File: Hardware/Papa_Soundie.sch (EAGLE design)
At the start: 80 parts, among them J1 Audio Jack, J2 MICRO-SD_CARD_SOCKET, U1 ATMEGA328P_TQFP, U2 VS1000D, U3 3.3V, U4 4MB Flash, Y1 12MHz, Y2 8MHz

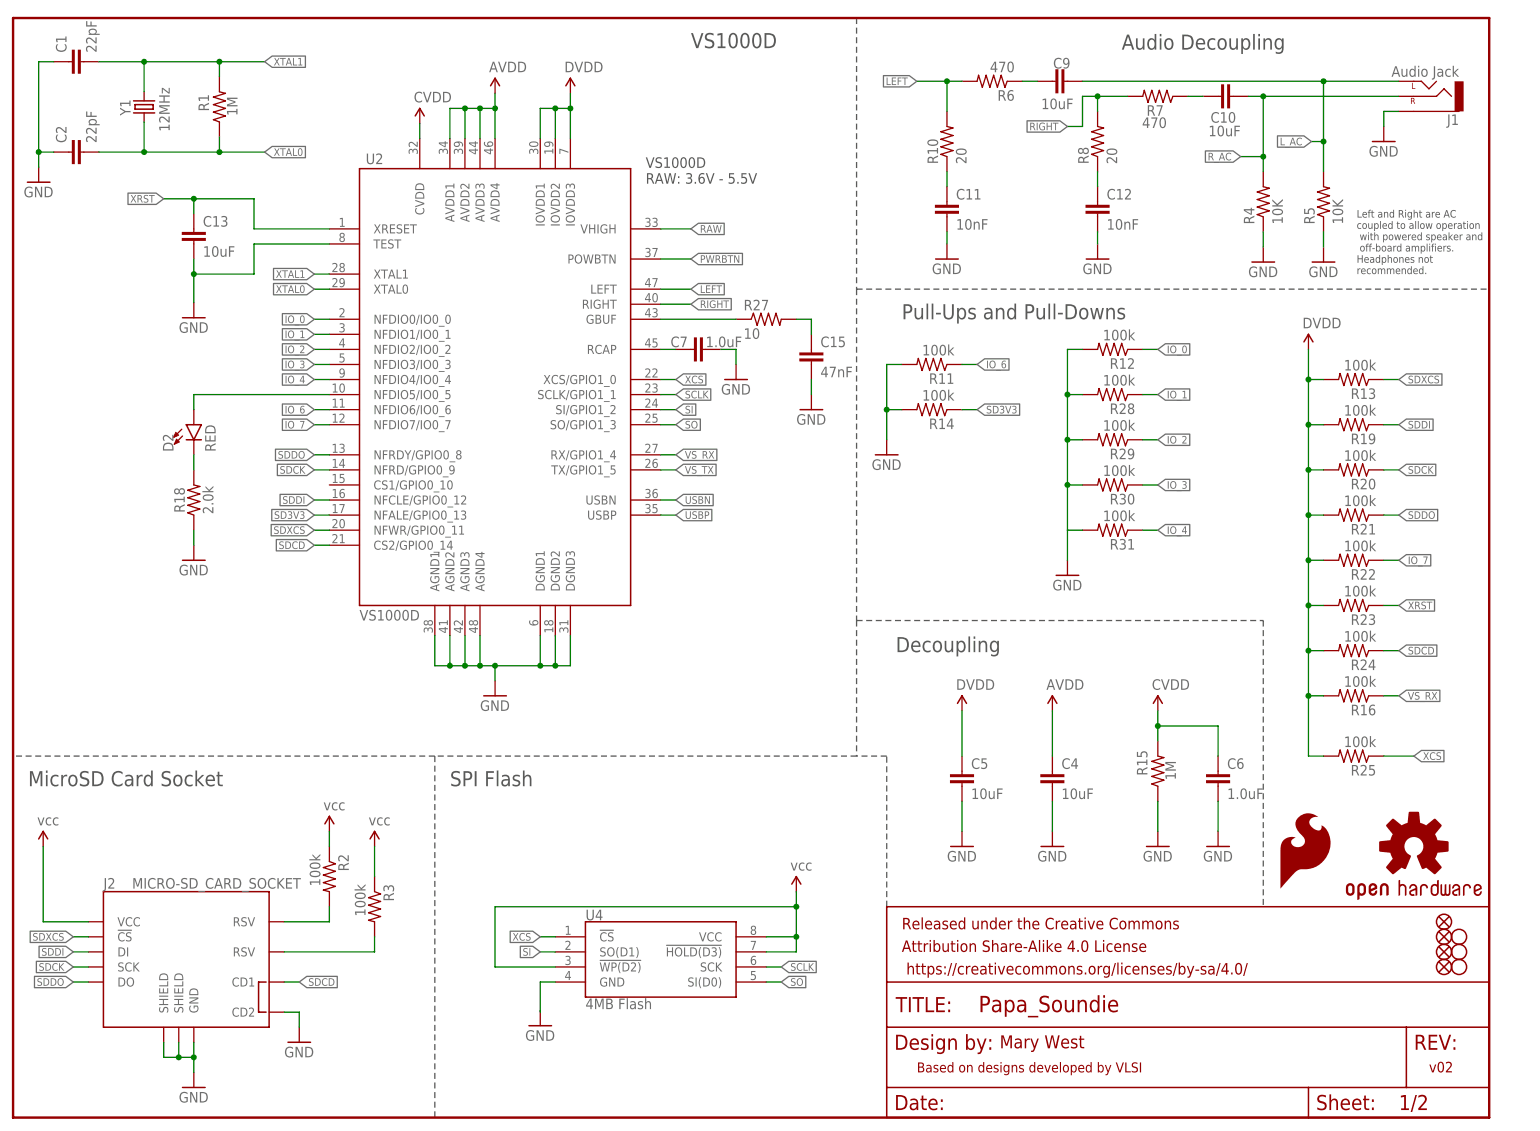
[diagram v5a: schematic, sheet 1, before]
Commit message: Updated Version No., removed ground connection from SD Card, v03
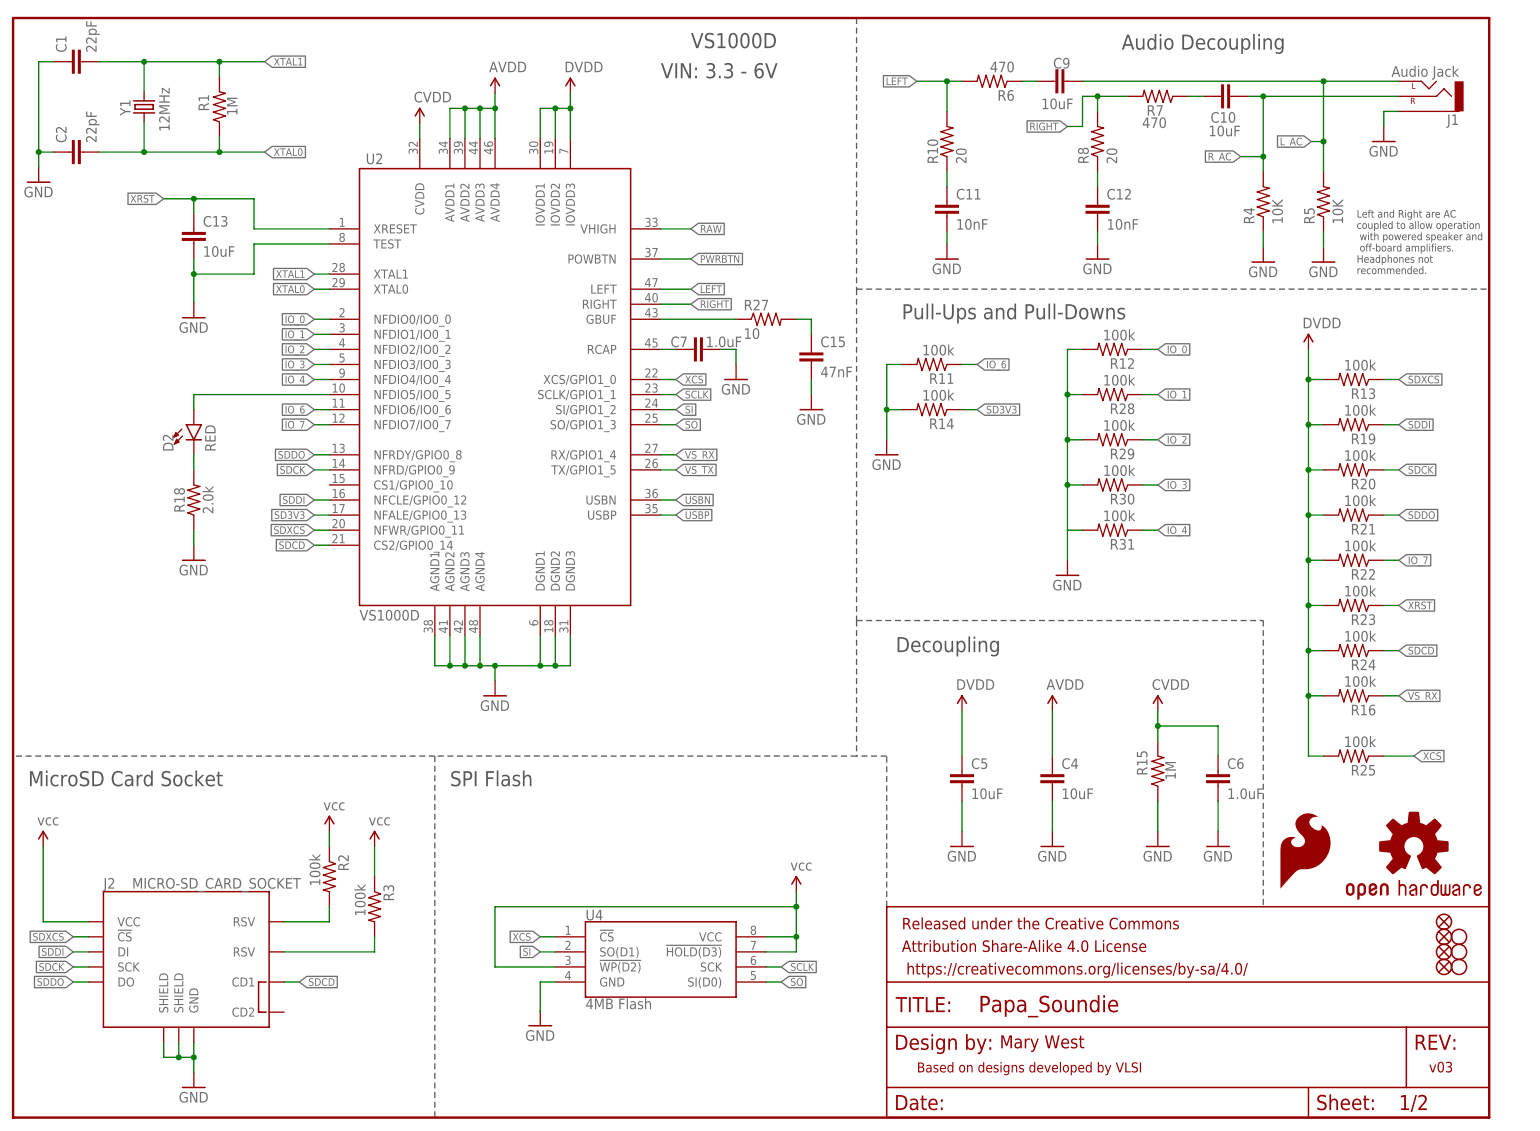
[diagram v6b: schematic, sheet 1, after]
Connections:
- net GND: no longer J2.CD2
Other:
- note added: "VIN: 3.3 - 6V"
- note added: "v03"
- note removed: "VS1000D RAW: 3.6V - 5.5V"
- note removed: "v02"
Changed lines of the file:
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@@
 <?xml version="1.0" encoding="utf-8"?>
 <!DOCTYPE eagle SYSTEM "eagle.dtd">
-<eagle version="8.5.1">
+<eagle version="7.7.0">
 <drawing>
 <settings>
 <setting alwaysvectorfont="no"/>
-<setting keepoldvectorfont="yes"/>
 <setting verticaltext="up"/>
 </settings>
@@
 <part name="H3" library="SparkFun-Electromechanical" deviceset="STAND-OFF" device="TIGHT"/>
 <part name="GND13" library="SparkFun-PowerSymbols" deviceset="GND" device=""/>
-<part name="GND21" library="SparkFun-Aesthetics" deviceset="GND" device=""/>
 <part name="D2" library="SparkFun-LED" deviceset="LED-RED" device="0603" value="RED"/>
 <part name="R18" library="SparkFun-Resistors" deviceset="2.0KOHM" device="-0603-1/10W-5%" value="2.0k"/>
@@
 <plain>
 <text x="166.37" y="11.684" size="2.1844" layer="94" font="vector">Mary West</text>
-<text x="238.76" y="7.62" size="1.778" layer="94" font="vector">v02</text>
+<text x="238.76" y="7.62" size="1.778" layer="94" font="vector">v03</text>
 <wire x1="0" y1="60.96" x2="0" y2="63.5" width="0.1524" layer="97" style="shortdash"/>
 <text x="148.844" y="78.486" size="2.54" layer="97" font="vector" ratio="10">Decoupling</text>
@@
 <wire x1="142.24" y1="185.42" x2="142.24" y2="139.7" width="0.1524" layer="97" style="longdash"/>
 <wire x1="142.24" y1="139.7" x2="248.92" y2="139.7" width="0.1524" layer="97" style="longdash"/>
-<text x="106.68" y="157.48" size="1.778" layer="97" font="vector">VS1000D
-RAW: 3.6V - 5.5V</text>
 <text x="2.54" y="55.88" size="2.54" layer="97" font="vector" ratio="10">MicroSD Card Socket</text>
 <text x="149.86" y="134.62" size="2.54" layer="97" font="vector" ratio="10">Pull-Ups and Pull-Downs</text>
@@
 <text x="73.66" y="55.88" size="2.54" layer="97" font="vector" ratio="10">SPI Flash</text>
 <text x="114.3" y="180.34" size="2.54" layer="97" font="vector" ratio="10">VS1000D</text>
+<text x="109.22" y="175.26" size="2.54" layer="97" font="vector">VIN: 3.3 - 6V</text>
 </plain>
 <instances>
@@
 <instance part="R25" gate="G$1" x="226.06" y="60.96" rot="R180"/>
 <instance part="H3" gate="G$1" x="243.84" y="27.94"/>
-<instance part="GND21" gate="1" x="48.26" y="12.7"/>
 <instance part="D2" gate="G$1" x="30.48" y="116.84"/>
 <instance part="R18" gate="G$1" x="30.48" y="104.14" rot="R90"/>
@@
 <pinref part="GND20" gate="1" pin="GND"/>
 <wire x1="88.9" y1="18.034" x2="88.9" y2="17.78" width="0.1524" layer="91"/>
-</segment>
-<segment>
-<pinref part="J2" gate="1" pin="CD2"/>
-<wire x1="45.72" y1="17.78" x2="48.26" y2="17.78" width="0.1524" layer="91"/>
-<wire x1="48.26" y1="17.78" x2="48.26" y2="15.24" width="0.1524" layer="91"/>
-<pinref part="GND21" gate="1" pin="GND"/>
 </segment>
 <segment>
@@
 <text x="58.42" y="177.8" size="5.08" layer="97" font="vector" ratio="10">Arduino Control</text>
 <text x="166.624" y="12.192" size="2.032" layer="94">Mary West</text>
-<text x="237.744" y="7.112" size="2.032" layer="94">v02</text>
+<text x="237.744" y="7.112" size="2.032" layer="94">v03</text>
 <wire x1="119.38" y1="185.42" x2="127" y2="185.42" width="0.1524" layer="97" style="longdash"/>
 <wire x1="127" y1="185.42" x2="127" y2="114.3" width="0.1524" layer="97" style="longdash"/>
@@
 <wire x1="30.48" y1="165.1" x2="33.02" y2="165.1" width="0.1524" layer="91"/>
 <label x="33.02" y="165.1" size="1.27" layer="95" xref="yes"/>
-</segment>
-<segment>
+<junction x="30.48" y="160.02"/>
+</segment>
+<segment>

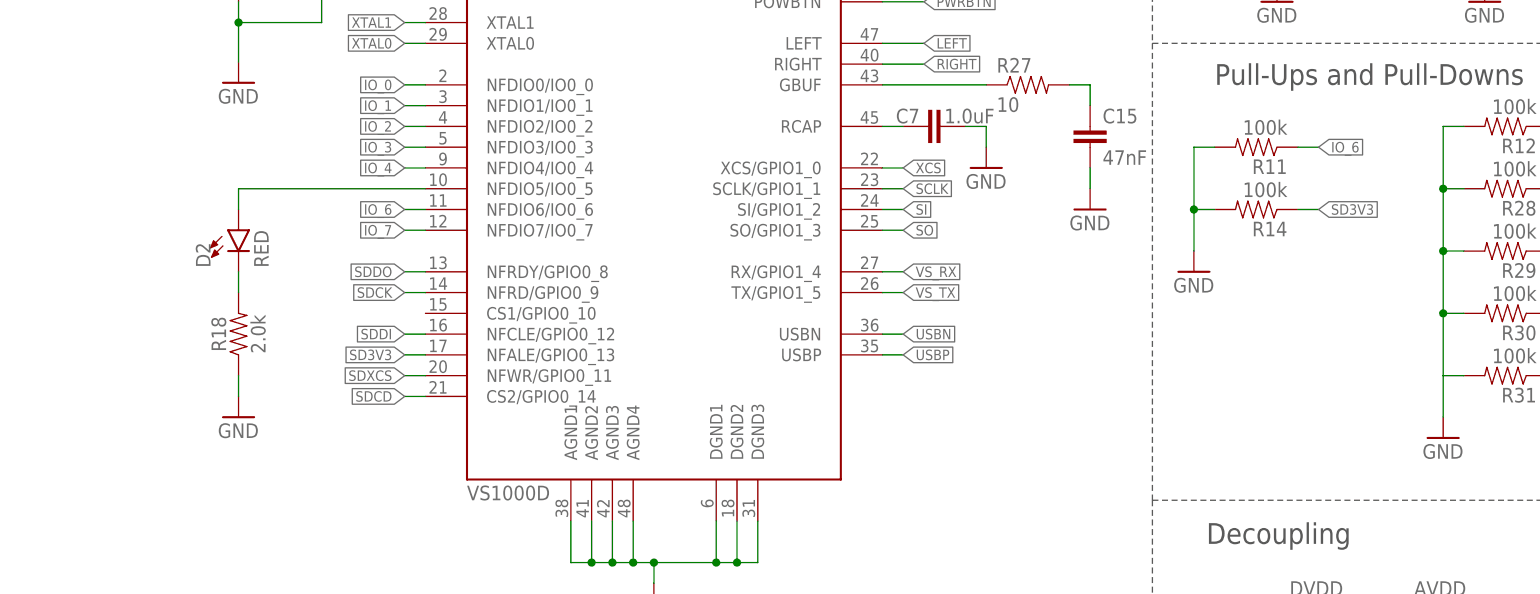
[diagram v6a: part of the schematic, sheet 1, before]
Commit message: fixing enable line, SD3V3
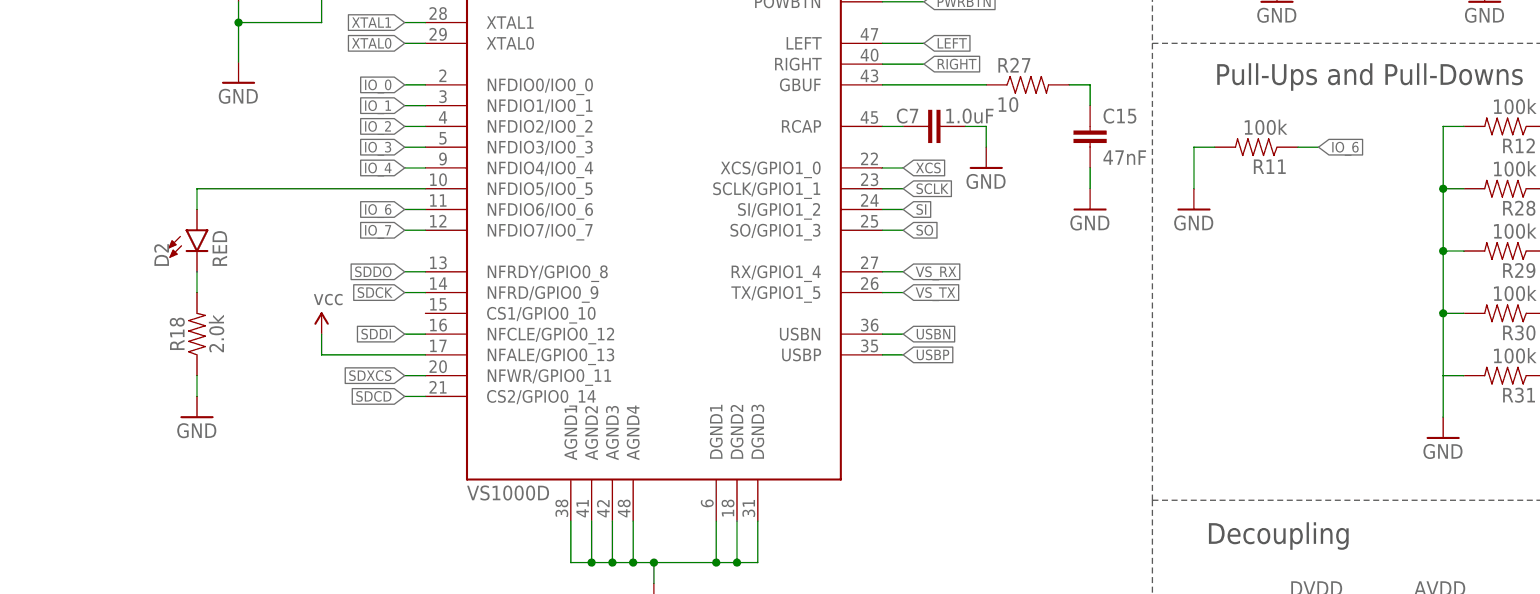
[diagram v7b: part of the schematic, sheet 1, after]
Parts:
- removed R14: 100k, SparkFun-Resistors:100KOHM-1/10W-1%(0603)
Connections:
- removed net SD3V3: R14.1, U2.NFALE/GPIO0_13, U3.EN
- net GND: no longer R14.2
- net RAW: now also U3.EN
- net VCC: now also U2.NFALE/GPIO0_13
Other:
- moved on the sheet: D2, R18
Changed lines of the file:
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@@
 <?xml version="1.0" encoding="utf-8"?>
 <!DOCTYPE eagle SYSTEM "eagle.dtd">
-<eagle version="7.7.0">
+<eagle version="8.6.1">
 <drawing>
 <settings>
 <setting alwaysvectorfont="no"/>
+<setting keepoldvectorfont="yes"/>
 <setting verticaltext="up"/>
 </settings>
@@
 <part name="SUPPLY16" library="SparkFun-Aesthetics" deviceset="VCC" device="" value="vcc"/>
 <part name="R11" library="SparkFun-Resistors" deviceset="100KOHM-1/10W-1%(0603)" device="" value="100k"/>
-<part name="R14" library="SparkFun-Resistors" deviceset="100KOHM-1/10W-1%(0603)" device="" value="100k"/>
 <part name="GND28" library="SparkFun-Aesthetics" deviceset="GND" device=""/>
 <part name="GND35" library="SparkFun-Aesthetics" deviceset="GND" device=""/>
@@
 <part name="GND30" library="SparkFun-PowerSymbols" deviceset="GND" device=""/>
 <part name="J12" library="SparkFun-Connectors" deviceset="CONN_01" device=""/>
+<part name="SUPPLY14" library="SparkFun-Aesthetics" deviceset="VCC" device="" value="vcc"/>
 </parts>
 <sheets>
@@
 <instance part="SUPPLY16" gate="G$1" x="60.96" y="45.72"/>
 <instance part="R11" gate="G$1" x="154.94" y="127" rot="R180"/>
-<instance part="R14" gate="G$1" x="154.94" y="119.38" rot="R180"/>
-<instance part="GND28" gate="1" x="147.32" y="111.76"/>
+<instance part="GND28" gate="1" x="147.32" y="119.38"/>
 <instance part="GND35" gate="1" x="30.48" y="134.874"/>
 <instance part="R12" gate="G$1" x="185.42" y="129.54" rot="R180"/>
@@
 <instance part="R25" gate="G$1" x="226.06" y="60.96" rot="R180"/>
 <instance part="H3" gate="G$1" x="243.84" y="27.94"/>
-<instance part="D2" gate="G$1" x="30.48" y="116.84"/>
-<instance part="R18" gate="G$1" x="30.48" y="104.14" rot="R90"/>
-<instance part="GND23" gate="1" x="30.48" y="93.98"/>
+<instance part="D2" gate="G$1" x="25.4" y="116.84"/>
+<instance part="R18" gate="G$1" x="25.4" y="104.14" rot="R90"/>
+<instance part="GND23" gate="1" x="25.4" y="93.98"/>
+<instance part="SUPPLY14" gate="G$1" x="40.64" y="104.14"/>
 </instances>
 <busses>
@@
 <pinref part="R11" gate="G$1" pin="2"/>
 <wire x1="149.86" y1="127" x2="147.32" y2="127" width="0.1524" layer="91"/>
-<wire x1="147.32" y1="127" x2="147.32" y2="119.38" width="0.1524" layer="91"/>
+<wire x1="147.32" y1="127" x2="147.32" y2="121.92" width="0.1524" layer="91"/>
 <pinref part="GND28" gate="1" pin="GND"/>
-<pinref part="R14" gate="G$1" pin="2"/>
-<wire x1="147.32" y1="119.38" x2="147.32" y2="114.3" width="0.1524" layer="91"/>
-<wire x1="147.32" y1="119.38" x2="149.86" y2="119.38" width="0.1524" layer="91"/>
-<junction x="147.32" y="119.38"/>
 </segment>
 <segment>
@@
 <pinref part="R18" gate="G$1" pin="1"/>
 <pinref part="GND23" gate="1" pin="GND"/>
-<wire x1="30.48" y1="99.06" x2="30.48" y2="96.52" width="0.1524" layer="91"/>
+<wire x1="25.4" y1="99.06" x2="25.4" y2="96.52" width="0.1524" layer="91"/>
 </segment>
 </net>
@@
 <pinref part="SUPPLY11" gate="G$1" pin="VCC"/>
 </segment>
+<segment>
+<pinref part="U2" gate="G$1" pin="NFALE/GPIO0_13"/>
+<wire x1="53.34" y1="101.6" x2="40.64" y2="101.6" width="0.1524" layer="91"/>
+<wire x1="40.64" y1="101.6" x2="40.64" y2="104.14" width="0.1524" layer="91"/>
+<pinref part="SUPPLY14" gate="G$1" pin="VCC"/>
+</segment>
 </net>
 <net name="AVDD" class="0">
@@
 </segment>
 </net>
-<net name="SD3V3" class="0">
-<segment>
-<pinref part="U2" gate="G$1" pin="NFALE/GPIO0_13"/>
-<wire x1="53.34" y1="101.6" x2="50.8" y2="101.6" width="0.1524" layer="91"/>
-<label x="50.8" y="101.6" size="1.27" layer="95" font="vector" rot="R180" xref="yes"/>
-</segment>
-<segment>
-<pinref part="R14" gate="G$1" pin="1"/>
-<wire x1="160.02" y1="119.38" x2="162.56" y2="119.38" width="0.1524" layer="91"/>
-<label x="162.56" y="119.38" size="1.27" layer="95" font="vector" xref="yes"/>
-</segment>
-</net>
 <net name="SDXCS" class="0">
 <segment>
@@
 <pinref part="D2" gate="G$1" pin="C"/>
 <pinref part="R18" gate="G$1" pin="2"/>
-<wire x1="30.48" y1="111.76" x2="30.48" y2="109.22" width="0.1524" layer="91"/>
+<wire x1="25.4" y1="111.76" x2="25.4" y2="109.22" width="0.1524" layer="91"/>
 </segment>
 </net>
@@
 <segment>
 <pinref part="U2" gate="G$1" pin="NFDIO5/IO0_5"/>
-<wire x1="53.34" y1="121.92" x2="30.48" y2="121.92" width="0.1524" layer="91"/>
+<wire x1="53.34" y1="121.92" x2="25.4" y2="121.92" width="0.1524" layer="91"/>
 <pinref part="D2" gate="G$1" pin="A"/>
-<wire x1="30.48" y1="121.92" x2="30.48" y2="119.38" width="0.1524" layer="91"/>
+<wire x1="25.4" y1="121.92" x2="25.4" y2="119.38" width="0.1524" layer="91"/>
 </segment>
 </net>
@@
 <segment>
 <pinref part="U3" gate="G$1" pin="IN"/>
-<wire x1="175.26" y1="160.02" x2="149.86" y2="160.02" width="0.1524" layer="91"/>
+<wire x1="175.26" y1="160.02" x2="165.1" y2="160.02" width="0.1524" layer="91"/>
 <label x="147.32" y="160.02" size="1.27" layer="95" font="vector" rot="R180" xref="yes"/>
 <pinref part="C3" gate="G$1" pin="1"/>
+<wire x1="165.1" y1="160.02" x2="149.86" y2="160.02" width="0.1524" layer="91"/>
 <wire x1="149.86" y1="160.02" x2="147.32" y2="160.02" width="0.1524" layer="91"/>
 <wire x1="149.86" y1="157.48" x2="149.86" y2="160.02" width="0.1524" layer="91"/>
 <junction x="149.86" y="160.02"/>
+<pinref part="U3" gate="G$1" pin="EN"/>
+<wire x1="175.26" y1="154.94" x2="165.1" y2="154.94" width="0.1524" layer="91"/>
+<wire x1="165.1" y1="154.94" x2="165.1" y2="160.02" width="0.1524" layer="91"/>
+<junction x="165.1" y="160.02"/>
 </segment>
 <segment>
@@
 </segment>
 </net>
-<net name="SD3V3" class="0">
-<segment>
-<pinref part="U3" gate="G$1" pin="EN"/>
-<wire x1="175.26" y1="154.94" x2="167.64" y2="154.94" width="0.1524" layer="91"/>
-<label x="167.64" y="154.94" size="1.27" layer="95" font="vector" rot="R180" xref="yes"/>
-</segment>
-</net>

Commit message: updated version no V10
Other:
- note added: "VIN: 3.3 - 9V"
- note added: "v10"
- note removed: "VIN: 3.3 - 6V"
- note removed: "v03"
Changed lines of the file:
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@@
 <?xml version="1.0" encoding="utf-8"?>
 <!DOCTYPE eagle SYSTEM "eagle.dtd">
-<eagle version="8.6.1">
+<eagle version="7.2.0">
 <drawing>
 <settings>
 <setting alwaysvectorfont="no"/>
-<setting keepoldvectorfont="yes"/>
 <setting verticaltext="up"/>
 </settings>
@@
 <plain>
 <text x="166.37" y="11.684" size="2.1844" layer="94" font="vector">Mary West</text>
-<text x="238.76" y="7.62" size="1.778" layer="94" font="vector">v03</text>
+<text x="238.76" y="7.62" size="1.778" layer="94" font="vector">v10</text>
 <wire x1="0" y1="60.96" x2="0" y2="63.5" width="0.1524" layer="97" style="shortdash"/>
 <text x="148.844" y="78.486" size="2.54" layer="97" font="vector" ratio="10">Decoupling</text>
@@
 <text x="73.66" y="55.88" size="2.54" layer="97" font="vector" ratio="10">SPI Flash</text>
 <text x="114.3" y="180.34" size="2.54" layer="97" font="vector" ratio="10">VS1000D</text>
-<text x="109.22" y="175.26" size="2.54" layer="97" font="vector">VIN: 3.3 - 6V</text>
+<text x="109.22" y="175.26" size="2.54" layer="97" font="vector">VIN: 3.3 - 9V</text>
 </plain>
 <instances>
@@
 <text x="58.42" y="177.8" size="5.08" layer="97" font="vector" ratio="10">Arduino Control</text>
 <text x="166.624" y="12.192" size="2.032" layer="94">Mary West</text>
-<text x="237.744" y="7.112" size="2.032" layer="94">v03</text>
+<text x="237.744" y="7.112" size="2.032" layer="94">v10</text>
 <wire x1="119.38" y1="185.42" x2="127" y2="185.42" width="0.1524" layer="97" style="longdash"/>
 <wire x1="127" y1="185.42" x2="127" y2="114.3" width="0.1524" layer="97" style="longdash"/>
